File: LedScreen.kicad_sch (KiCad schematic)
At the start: 27 parts, among them U1 Teensy4.1, U2 74HCT245

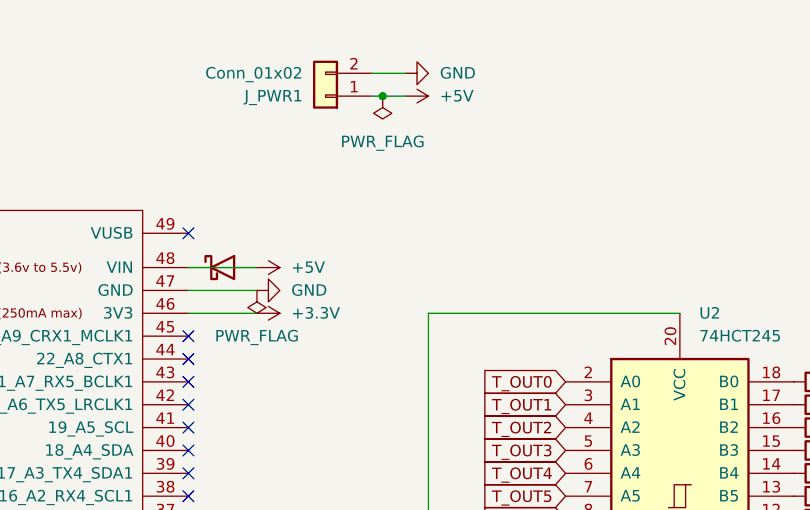
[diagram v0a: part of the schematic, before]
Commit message: added caps to 5v + gnd
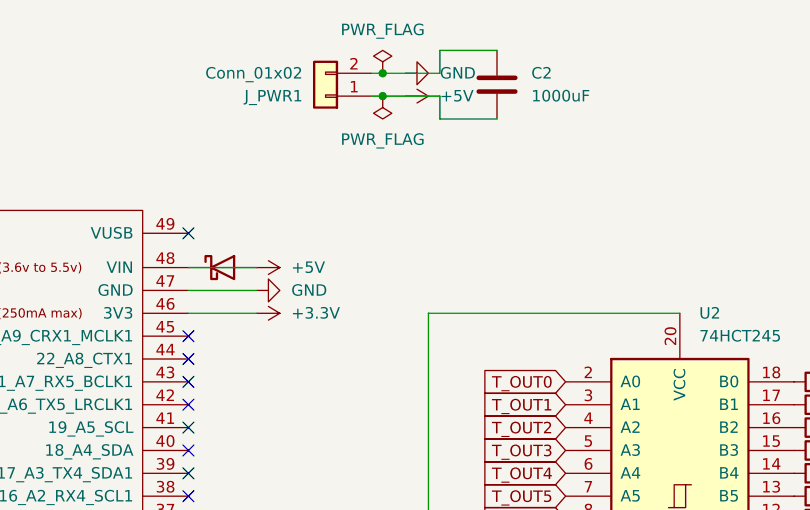
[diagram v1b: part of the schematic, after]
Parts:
- added C2: 1000uF, symbol Device:C
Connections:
- net +5V: now also C2.2
- net GND: now also C2.1
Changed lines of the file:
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@@
 	)
 	(junction
+		(at 139.7 36.83)
+		(diameter 0)
+		(color 0 0 0 0)
+	)
+	(junction
 		(at 139.7 39.37)
 		(diameter 0)
@@
 	(wire
 		(pts
-			(xy 142.24 36.83) (xy 138.43 36.83)
+			(xy 138.43 36.83) (xy 139.7 36.83)
 		)
 		(stroke
@@
 	(wire
 		(pts
-			(xy 118.11 60.96) (xy 125.73 60.96)
+			(xy 139.7 36.83) (xy 142.24 36.83)
 		)
 		(stroke
@@
 	(wire
 		(pts
-			(xy 118.11 63.5) (xy 125.73 63.5)
+			(xy 152.4 41.91) (xy 146.05 41.91)
+		)
+		(stroke
+			(width 0)
+			(type default)
+		)
+	)
+	(wire
+		(pts
+			(xy 146.05 41.91) (xy 146.05 39.37)
+		)
+		(stroke
+			(width 0)
+			(type default)
+		)
+	)
+	(wire
+		(pts
+			(xy 146.05 39.37) (xy 142.24 39.37)
+		)
+		(stroke
+			(width 0)
+			(type default)
+		)
+	)
+	(wire
+		(pts
+			(xy 152.4 34.29) (xy 146.05 34.29)
+		)
+		(stroke
+			(width 0)
+			(type default)
+		)
+	)
+	(wire
+		(pts
+			(xy 146.05 34.29) (xy 146.05 36.83)
+		)
+		(stroke
+			(width 0)
+			(type default)
+		)
+	)
+	(wire
+		(pts
+			(xy 146.05 36.83) (xy 142.24 36.83)
 		)
 		(stroke
@@
 	(wire
 		(pts
+			(xy 118.11 60.96) (xy 125.73 60.96)
+		)
+		(stroke
+			(width 0)
+			(type default)
+		)
+	)
+	(wire
+		(pts
+			(xy 118.11 63.5) (xy 125.73 63.5)
+		)
+		(stroke
+			(width 0)
+			(type default)
+		)
+	)
+	(wire
+		(pts
 			(xy 144.78 97.79) (xy 142.24 97.79)
 		)
@@
 	)
 	(symbol
+		(lib_id "power:PWR_FLAG")
+		(at 139.7 36.83 0)
+		(unit 1)
+		(exclude_from_sim no)
+		(in_bom yes)
+		(on_board yes)
+		(dnp no)
+		(property "Reference" "#FLG02"
+			(at 139.7 34.925 0)
+			(effects
+				(font
+					(size 1.27 1.27)
+				)
+				(hide yes)
+			)
+		)
+		(property "Value" "PWR_FLAG"
+			(at 139.7 32.004 0)
+			(effects
+				(font
+					(size 1.27 1.27)
+				)
+			)
+		)
+		(property "Footprint" ""
+			(at 139.7 36.83 0)
+			(effects
+				(font
+					(size 1.27 1.27)
+				)
+				(hide yes)
+			)
+		)
+		(property "Datasheet" "~"
+			(at 139.7 36.83 0)
+			(effects
+				(font
+					(size 1.27 1.27)
+				)
+				(hide yes)
+			)
+		)
+		(property "Description" "Special symbol for telling ERC where power comes from"
+			(at 139.7 36.83 0)
+			(effects
+				(font
+					(size 1.27 1.27)
+				)
+				(hide yes)
+			)
+		)
+		(pin "1"
+		)
+		(instances
+			(project "LedScreen"
+				(path "/6393ae6b-20d3-4709-8a4f-a83a956b3492"
+					(reference "#FLG02")
+					(unit 1)
+				)
+			)
+		)
+	)
+	(symbol
 		(lib_id "Connector_Generic:Conn_01x03")
 		(at 240.03 114.3 0)
@@
 		(on_board yes)
 		(dnp no)
-		(fields_autoplaced yes)
 		(property "Reference" "#FLG01"
 			(at 139.7 41.275 0)
@@
 		)
 		(property "Value" "PWR_FLAG"
-			(at 139.7 44.45 0)
+			(at 139.7 44.196 0)
 			(effects
 				(font
@@
 	)
 	(symbol
-		(lib_id "power:PWR_FLAG")
-		(at 125.73 60.96 180)
-		(unit 1)
-		(exclude_from_sim no)
-		(in_bom yes)
-		(on_board yes)
-		(dnp no)
-		(fields_autoplaced yes)
-		(property "Reference" "#FLG02"
-			(at 125.73 62.865 0)
-			(effects
-				(font
-					(size 1.27 1.27)
-				)
-				(hide yes)
-			)
-		)
-		(property "Value" "PWR_FLAG"
-			(at 125.73 66.04 0)
-			(effects
-				(font
-					(size 1.27 1.27)
-				)
-			)
-		)
-		(property "Footprint" ""
-			(at 125.73 60.96 0)
-			(effects
-				(font
-					(size 1.27 1.27)
-				)
-				(hide yes)
-			)
-		)
-		(property "Datasheet" "~"
-			(at 125.73 60.96 0)
-			(effects
-				(font
-					(size 1.27 1.27)
-				)
-				(hide yes)
-			)
-		)
-		(property "Description" "Special symbol for telling ERC where power comes from"
-			(at 125.73 60.96 0)
-			(effects
-				(font
-					(size 1.27 1.27)
-				)
-				(hide yes)
-			)
-		)
-		(pin "1"
-		)
-		(instances
-			(project "LedScreen"
-				(path "/6393ae6b-20d3-4709-8a4f-a83a956b3492"
-					(reference "#FLG02")
-					(unit 1)
-				)
-			)
-		)
-	)
-	(symbol
 		(lib_id "project_logic:74HCT245")
 		(at 172.72 83.82 0)
@@
 					(unit 1)
 				)
+			)
+		)
+	)
+	(symbol
+		(lib_id "Device:C")
+		(at 152.4 38.1 0)
+		(unit 1)
+		(exclude_from_sim no)
+		(in_bom yes)
+		(on_board yes)
+		(dnp no)
+		(fields_autoplaced yes)
+		(property "Reference" "C2"
+			(at 156.21 36.8299 0)
+			(effects
+				(font
+					(size 1.27 1.27)
+				)
+				(justify left)
+			)
+		)
+		(property "Value" "1000uF"
+			(at 156.21 39.3699 0)
+			(effects
+				(font
+					(size 1.27 1.27)
+				)
+				(justify left)
+			)
+		)
+		(property "Footprint" ""
+			(at 153.3652 41.91 0)
+			(effects
+				(font
+					(size 1.27 1.27)
+				)
+				(hide yes)
+			)
+		)
+		(property "Datasheet" "~"
+			(at 152.4 38.1 0)
+			(effects
+				(font
+					(size 1.27 1.27)
+				)
+				(hide yes)
+			)
+		)
+		(property "Description" "Unpolarized capacitor"
+			(at 152.4 38.1 0)
+			(effects
+				(font
+					(size 1.27 1.27)
+				)
+				(hide yes)
+			)
+		)
+		(pin "1"
+		)
+		(pin "2"
+		)
+		(instances
+			(project ""
+				(path "/6393ae6b-20d3-4709-8a4f-a83a956b3492"
+					(reference "C2")
+					(unit 1)
+				)

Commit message: DONE WIRINg
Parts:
- removed D1: D_Schottky, symbol Device:D_Schottky
- removed U1: Teensy4.1, teensy:Teensy41, symbol teensy_library:Teensy4.1
- added A1: RaspberryPi_Pico, Module:RaspberryPi_Pico_SMD_HandSolder, symbol MCU_Module:RaspberryPi_Pico_Debug
- added C3: 4.7uF, Capacitor_SMD:C_1206_3216Metric, symbol Device:C
- added GPIO1: Conn_01x13, Connector_PinHeader_2.54mm:PinHeader_1x13_P2.54mm_Vertical, symbol Connector_Generic:Conn_01x13
- added J_GPIO13: SPARE_GPIO_13, Connector_PinHeader_2.54mm:PinHeader_1x03_P2.54mm_Horizontal, symbol Connector_Generic:Conn_01x03
- added J_GPIO14: SPARE_GPIO_14, Connector_PinHeader_2.54mm:PinHeader_1x03_P2.54mm_Horizontal, symbol Connector_Generic:Conn_01x03
- added J_GPIO15: SPARE_GPIO_15, Connector_PinHeader_2.54mm:PinHeader_1x03_P2.54mm_Horizontal, symbol Connector_Generic:Conn_01x03
- added J_GPIO16: SPARE_GPIO_16, Connector_PinHeader_2.54mm:PinHeader_1x03_P2.54mm_Horizontal, symbol Connector_Generic:Conn_01x03
- added J_LED_5V1: Conn_01x01_Pin, Connector_PinHeader_1.00mm:PinHeader_1x01_P1.00mm_Vertical, symbol Connector:Conn_01x01_Pin
- added J_PWRA1, J_PWRA2, J_PWRA3, J_PWRA4, J_PWRA5: Conn_01x02, Connector_PinHeader_2.54mm:PinHeader_1x02_P2.54mm_Horizontal, symbol Connector_Generic:Conn_01x02
- added J_TP_PWR1: TP_PWR, Connector_PinHeader_2.54mm:PinHeader_1x03_P2.54mm_Horizontal, symbol Connector_Generic:Conn_01x03
- added J_TP_SIG1: TP_SIG, Connector_PinHeader_2.54mm:PinHeader_1x03_P2.54mm_Horizontal, symbol Connector_Generic:Conn_01x03
- added SD_READER1: Micro_SD_Card_Det_Hirose_DM3AT, Connector_Card:microSD_HC_Hirose_DM3AT-SF-PEJM5, symbol Connector:Micro_SD_Card_Det_Hirose_DM3AT
- 74HCT245: renamed from U2; footprint (none) -> Package_DIP:DIP-20_W7.62mm
- C1: footprint (none) -> Capacitor_SMD:C_0805_2012Metric
- C2: footprint (none) -> Capacitor_THT:CP_Radial_D10.0mm_P5.00mm
- J_LED0, J_LED1, J_LED2, J_LED3, J_LED4, J_LED5, J_LED6, J_LED7: footprint (none) -> Connector_PinHeader_2.54mm:PinHeader_1x03_P2.54mm_Horizontal
- J_MODE1: footprint (none) -> Connector_PinHeader_2.54mm:PinHeader_1x03_P2.54mm_Vertical
- J_PWR1, J_SYNC_IN1, J_SYNC_OUT1: footprint (none) -> Connector_PinHeader_2.54mm:PinHeader_1x02_P2.54mm_Horizontal
- R1, R2, R3, R4, R5, R6, R7, R8: value 330 -> 330 (0-330); footprint (none) -> Resistor_SMD:R_0805_2012Metric
- R_MODE_PD1, R_SYNC_PD1, R_SYNC_SER1: footprint (none) -> Resistor_SMD:R_0805_2012Metric
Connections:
- net +5V: now also A1.39 (VSYS), C3.2, J_PWRA1.1 (Pin_1), J_PWRA2.1 (Pin_1), J_PWRA3.1 (Pin_1), J_PWRA4.1 (Pin_1), J_PWRA5.1 (Pin_1), J_TP_PWR1.3 (Pin_3)
- net GND: now also J_SYNC_OUT1.2 (Pin_2), A1.13 (GND), A1.18 (GND), A1.23 (GND), A1.28 (GND), A1.3 (GND), A1.38 (GND), A1.8 (GND), A1.D2 (GND), C3.1, J_GPIO13.1 (Pin_1), J_GPIO14.1 (Pin_1), J_GPIO15.1 (Pin_1), J_GPIO16.1 (Pin_1), J_PWRA1.2 (Pin_2), J_PWRA2.2 (Pin_2), J_PWRA3.2 (Pin_2), J_PWRA4.2 (Pin_2), J_PWRA5.2 (Pin_2), J_TP_PWR1.1 (Pin_1), SD_READER1.11 (SHIELD), SD_READER1.6 (VSS); no longer J_SYNC_OUT1.1 (Pin_1)
- net LED0_DATA: now also J_TP_SIG1.2 (Pin_2)
- net MODE: now also A1.32 (GPIO27_ADC1)
- net T_OUT0: now also A1.1 (GPIO0), J_TP_SIG1.3 (Pin_3)
- net T_OUT1: now also A1.2 (GPIO1)
- net T_OUT2: now also A1.31 (GPIO26_ADC0)
- net T_OUT3: now also A1.34 (GPIO28_ADC2)
- net T_OUT4: now also A1.16 (GPIO12)
- net T_OUT5: now also A1.17 (GPIO13)
- net T_OUT6: now also A1.19 (GPIO14)
- net T_OUT7: now also A1.20 (GPIO15)
- net LED_PIN3: now reaches J_LED6.3 (Pin_3)
- net LED_PIN3: now also J_LED0.3 (Pin_3), J_LED1.3 (Pin_3), J_LED2.3 (Pin_3), J_LED3.3 (Pin_3), J_LED4.3 (Pin_3), J_LED5.3 (Pin_3), J_LED7.3 (Pin_3), J_LED_5V1.1 (Pin_1)
- net SYNC_OUT: now reaches R_SYNC_SER1.2
- net SYNC_OUT: now also J_SYNC_OUT1.1 (Pin_1), J_TP_SIG1.1 (Pin_1)
- net +3.3V renamed +3V3
- net +3V3: now also A1.36 (3V3), J_GPIO13.3 (Pin_3), J_GPIO14.3 (Pin_3), J_GPIO15.3 (Pin_3), J_GPIO16.3 (Pin_3), J_TP_PWR1.2 (Pin_2), SD_READER1.4 (VDD)
- net SYNC renamed SYNC_IN
- net SYNC_IN: now also A1.29 (GPIO22); no longer J_SYNC_OUT1.2 (Pin_2), R_SYNC_SER1.1
- new net 3V3_EN: A1.37 (3V3_EN), GPIO1.6 (Pin_6)
- new net ADC_VREF: A1.35 (ADC_VREF), GPIO1.2 (Pin_2)
- new net AGND: A1.33 (AGND), GPIO1.1 (Pin_1)
- new net GPIO10: A1.14 (GPIO10), GPIO1.11 (Pin_11)
- new net GPIO11: A1.15 (GPIO11), GPIO1.12 (Pin_12)
- new net GPIO16: A1.21 (GPIO16), GPIO1.13 (Pin_13)
- new net GPIO2: A1.4 (GPIO2), J_GPIO13.2 (Pin_2)
- new net GPIO3: A1.5 (GPIO3), J_GPIO14.2 (Pin_2)
- new net GPIO4: A1.6 (GPIO4), J_GPIO15.2 (Pin_2)
- new net GPIO5: A1.7 (GPIO5), J_GPIO16.2 (Pin_2)
- new net GPIO6: A1.9 (GPIO6), GPIO1.7 (Pin_7)
- new net GPIO7: A1.10 (GPIO7), GPIO1.8 (Pin_8)
- new net GPIO8: A1.11 (GPIO8), GPIO1.9 (Pin_9)
- new net GPIO9: A1.12 (GPIO9), GPIO1.10 (Pin_10)
- new net RUN: A1.30 (RUN), GPIO1.5 (Pin_5)
- new net SD_CS: A1.27 (GPIO21), SD_READER1.2 (DAT3/CD)
- new net SD_MISO: A1.26 (GPIO20), SD_READER1.7 (DAT0)
- new net SD_MOSI: A1.25 (GPIO19), SD_READER1.3 (CMD)
- new net SD_SCK: A1.24 (GPIO18), SD_READER1.5 (CLK)
- new net SWCLK: A1.D1 (SWCLK), GPIO1.3 (Pin_3)
- new net SWDIO: A1.D3 (SWDIO), GPIO1.4 (Pin_4)
- new net SYNC_OUT_DRV: A1.22 (GPIO17), R_SYNC_SER1.1
- no-connect marks 62 -> 5
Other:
- company: (none) -> Nick Esselman
- title: (none) -> Led Controler
- moved on the sheet: 74HCT245, C1, C2, J_LED0, J_LED1, J_LED2, J_LED3, J_LED4, J_LED5, J_LED6, J_LED7, J_MODE1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

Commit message: finsighed new v2 routing
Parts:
- removed J_PWR1, J_PWRA1, J_PWRA2, J_PWRA3, J_PWRA4, J_PWRA5: Conn_01x02, Connector_PinHeader_2.54mm:PinHeader_1x02_P2.54mm_Horizontal, symbol Connector_Generic:Conn_01x02
- added J_PWR1: Conn_01x03, Connector_JST:JST_XH_S3B-XH-SM4-TB_1x03-1MP_P2.50mm_Horizontal, symbol Connector_Generic:Conn_01x03
- added J_PWRA1: Conn_01x10, Connector_PinHeader_2.54mm:PinHeader_1x10_P2.54mm_Vertical, symbol Connector_Generic:Conn_01x10
- A1: footprint Module:RaspberryPi_Pico_SMD_HandSolder -> Module:RaspberryPi_Pico_Common_THT
- J_GPIO13, J_GPIO14, J_GPIO15, J_GPIO16, J_LED0, J_LED1, J_LED2, J_LED3, J_LED4, J_LED5, J_LED6, J_LED7: footprint Connector_PinHeader_2.54mm:PinHeader_1x03_P2.54mm_Horizontal -> Connector_JST:JST_XH_S3B-XH-SM4-TB_1x03-1MP_P2.50mm_Horizontal
- J_TP_PWR1, J_TP_SIG1: footprint Connector_PinHeader_2.54mm:PinHeader_1x03_P2.54mm_Horizontal -> Connector_PinHeader_2.54mm:PinHeader_1x03_P2.54mm_Vertical
- R1, R2, R3, R4, R5, R6, R7, R8: value 330 (0-330) -> 0R; footprint Resistor_SMD:R_0805_2012Metric -> Resistor_SMD:R_1206_3216Metric; DNP (none) -> Yes
- V5: renamed from J_LED_5V1; footprint Connector_PinHeader_1.00mm:PinHeader_1x01_P1.00mm_Vertical -> Connector_PinHeader_2.54mm:PinHeader_1x01_P2.54mm_Vertical
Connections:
- net +5V: now also J_PWR1.1 (Pin_1), J_PWRA1.1 (Pin_1), J_PWRA1.3 (Pin_3), J_PWRA1.5 (Pin_5), J_PWRA1.7 (Pin_7), J_PWRA1.9 (Pin_9)
- net GND: now also J_PWR1.2 (Pin_2), J_PWRA1.10 (Pin_10), J_PWRA1.2 (Pin_2), J_PWRA1.4 (Pin_4), J_PWRA1.6 (Pin_6), J_PWRA1.8 (Pin_8)
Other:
- note added: "Default 0R. Populate 220–330Ω if ringing or instability occurs."
- note added: "Optional series resistors for WS2812 signal integrity."
